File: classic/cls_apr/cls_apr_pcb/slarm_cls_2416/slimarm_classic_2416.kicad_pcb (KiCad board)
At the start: 2 copper layers, 3 parts, among them U1 s3c2416, U2 K4T1G164QJBCE7, U3 K9F5608U0C

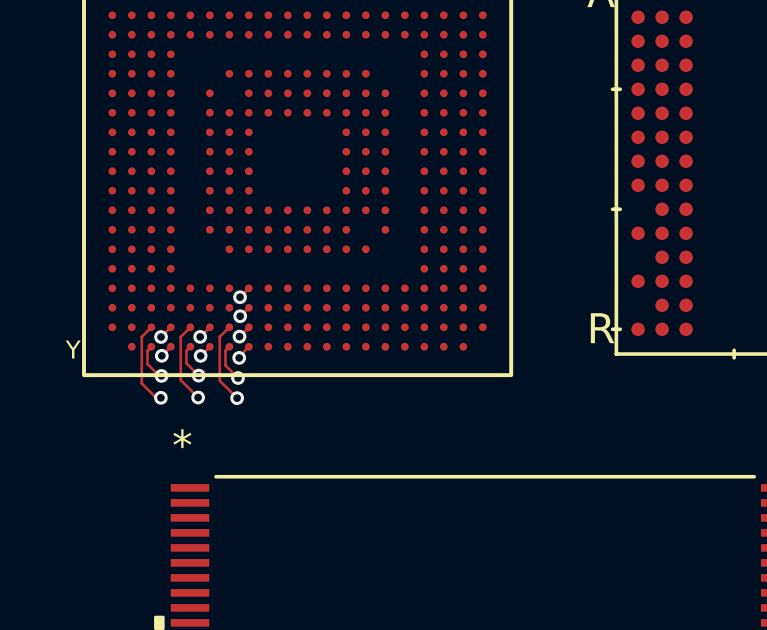
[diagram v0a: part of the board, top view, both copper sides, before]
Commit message: fixed carambola board; board 3d models
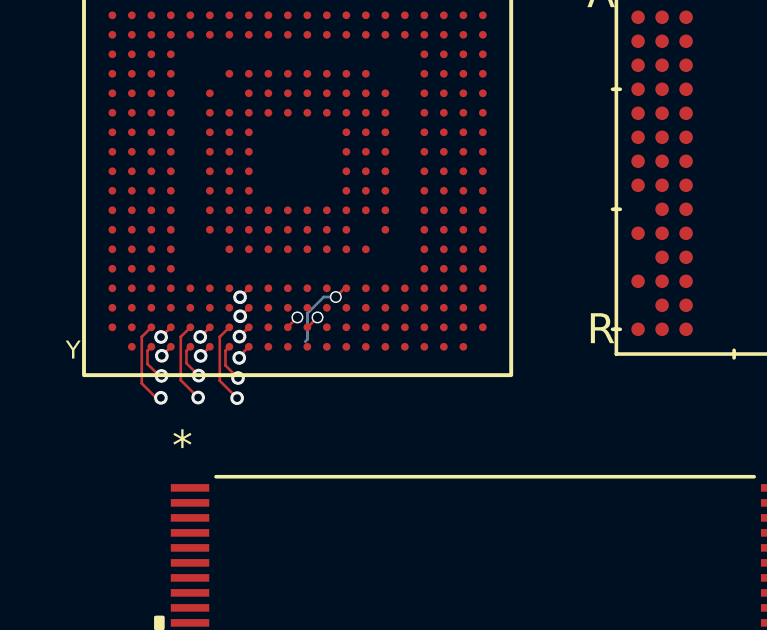
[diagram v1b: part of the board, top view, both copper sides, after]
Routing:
- net unconnected-(U1-PadU13): track 0.00 -> 2.62 mm, vias 0 -> 1
- net unconnected-(U1-PadW11): track 0.00 -> 0.48 mm, vias 0 -> 1
- net unconnected-(U1-PadW10): track 0.00 -> 0.46 mm, vias 0 -> 1
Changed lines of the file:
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@@
   (segment (start 21.96 28.579434) (end 21.957147 28.576581) (width 0.0889) (layer "F.Cu") (net 260))
   (via (at 21.957147 28.576581) (size 0.4572) (drill 0.254) (layers "F.Cu" "B.Cu") (net 260))
+  (segment (start 25.441245 28.2788) (end 25.150023 28.570022) (width 0.0889) (layer "F.Cu") (net 265))
+  (segment (start 25.501 28.2788) (end 25.441245 28.2788) (width 0.0889) (layer "F.Cu") (net 265))
+  (via (at 25.150023 28.570022) (size 0.4) (drill 0.3) (layers "F.Cu" "B.Cu") (net 265))
+  (segment (start 24.20665 29.108621) (end 24.20665 29.98335) (width 0.0889) (layer "B.Cu") (net 265))
+  (segment (start 24.745249 28.570022) (end 24.20665 29.108621) (width 0.0889) (layer "B.Cu") (net 265))
+  (segment (start 25.150023 28.570022) (end 24.745249 28.570022) (width 0.0889) (layer "B.Cu") (net 265))
+  (segment (start 24.20665 29.98335) (end 24.13 30.06) (width 0.0889) (layer "B.Cu") (net 265))
   (segment (start 22.251 28.9288) (end 21.9698 29.21) (width 0.0889) (layer "F.Cu") (net 280))
   (segment (start 21.9698 29.21) (end 21.960457 29.21) (width 0.0889) (layer "F.Cu") (net 280))
@@
   (segment (start 22.251 29.5788) (end 21.94 29.8898) (width 0.0889) (layer "F.Cu") (net 300))
   (via (at 21.94 29.89) (size 0.4572) (drill 0.254) (layers "F.Cu" "B.Cu") (net 300))
+  (segment (start 23.551 29.569) (end 23.87 29.25) (width 0.0889) (layer "F.Cu") (net 302))
+  (segment (start 23.551 29.5788) (end 23.551 29.569) (width 0.0889) (layer "F.Cu") (net 302))
+  (via (at 23.87 29.25) (size 0.4) (drill 0.3) (layers "F.Cu" "B.Cu") (net 302))
+  (segment (start 24.2112 29.5788) (end 24.54 29.25) (width 0.0889) (layer "F.Cu") (net 303))
+  (segment (start 24.201 29.5788) (end 24.2112 29.5788) (width 0.0889) (layer "F.Cu") (net 303))
+  (via (at 24.54 29.25) (size 0.4) (drill 0.3) (layers "F.Cu" "B.Cu") (net 303))
   (segment (start 19.001 30.2288) (end 18.872 30.3578) (width 0.0889) (layer "F.Cu") (net 314))
   (segment (start 19.25 31.18) (end 19.32 31.18) (width 0.0889) (layer "F.Cu") (net 314))
